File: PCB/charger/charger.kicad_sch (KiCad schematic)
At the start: 18 parts, among them J1 Conn_01x02_Socket, J2 USB_C_Receptacle, J3 Conn_01x02_Socket, J4 Conn_01x02_Socket, J5 Conn_01x02_Socket, Q2 BSS83P, U1 MCP73831T-2ACI/OT

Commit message: idk
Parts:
- D1, D2: footprint LED_SMD:LED_0402_1005Metric -> LED_SMD:LED_0603_1608Metric
- R5: value 10K\ -> 10K
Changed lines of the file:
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@@
 			)
 		)
-		(property "Value" "10K\\"
+		(property "Value" "10K"
 			(at 217.17 68.58 0)
 			(effects
@@
 		)
 		(property "Footprint" "Resistor_SMD:R_0402_1005Metric"
-			(at 217.17 68.58 0)
+			(at 217.424 71.882 0)
 			(effects
 				(font
@@
 			)
 		)
-		(property "Footprint" "LED_SMD:LED_0402_1005Metric"
+		(property "Footprint" "LED_SMD:LED_0603_1608Metric"
 			(at 160.02 78.74 0)
 			(effects
@@
 			)
 		)
-		(property "Footprint" "LED_SMD:LED_0402_1005Metric"
+		(property "Footprint" "LED_SMD:LED_0603_1608Metric"
 			(at 160.02 71.12 0)
 			(effects

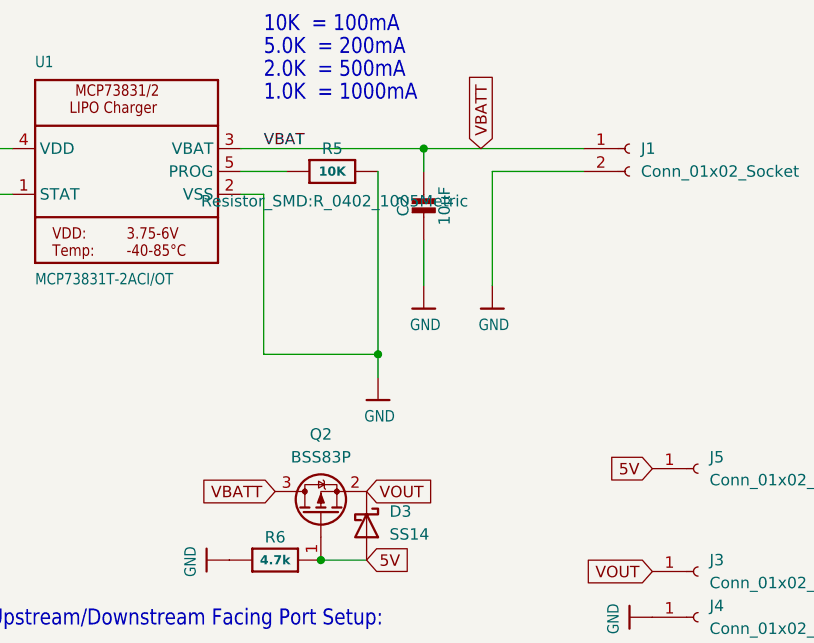
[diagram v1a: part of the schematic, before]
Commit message: reorganizing repo
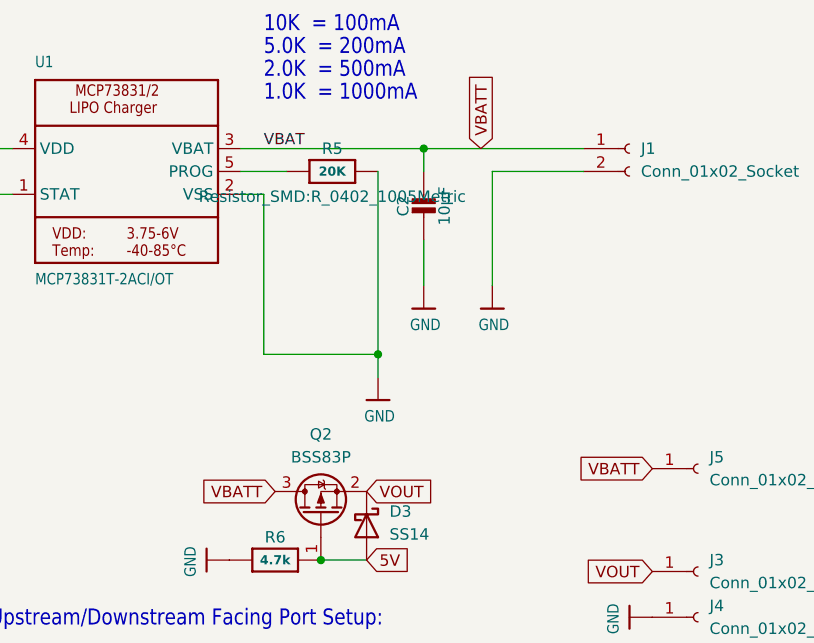
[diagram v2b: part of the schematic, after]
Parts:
- R5: value 10K -> 20K
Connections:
- net 5V: no longer J5.1 (Pin_1)
- net VBATT: now also J5.1 (Pin_1)
